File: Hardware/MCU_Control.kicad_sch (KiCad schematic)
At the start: 19 parts, among them J1 USB2.0_16P, Q3 BC817, Q4 BC817, SW1 ENABLE, U15 CH340C, U4 ESP32-WROOM-32E, U5 USBLC6-2SC6

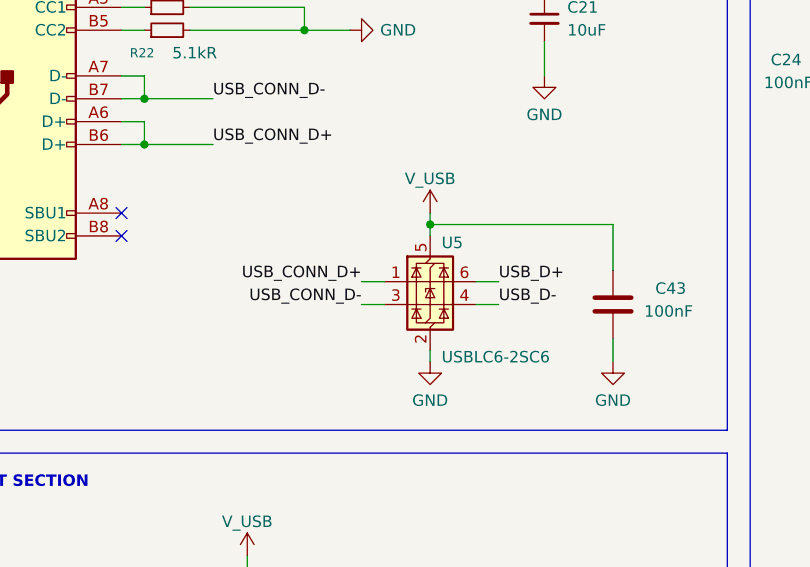
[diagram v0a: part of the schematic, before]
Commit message: fix(hardware): reroute PCB for schematic updates
Synchronize PCB routing and net assignments with the revised optocoupler control design, including related auxiliary power and USB signal wiring updates.
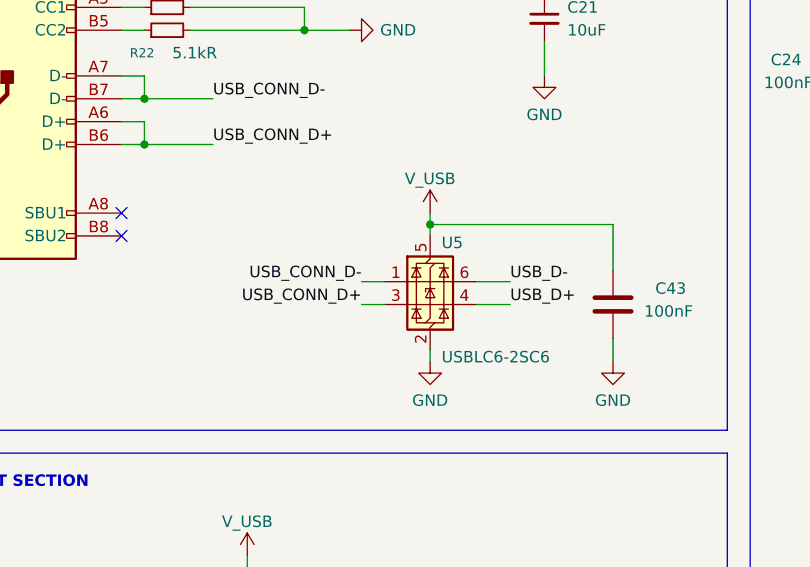
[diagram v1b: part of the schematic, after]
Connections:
- net USB_CONN_D+: now also U5.3 (I/O2); no longer U5.1 (I/O1)
- net USB_CONN_D-: now also U5.1 (I/O1); no longer U5.3 (I/O2)
- net USB_D+: now also U5.4 (I/O2); no longer U5.6 (I/O1)
- net USB_D-: now also U5.6 (I/O1); no longer U5.4 (I/O2)
